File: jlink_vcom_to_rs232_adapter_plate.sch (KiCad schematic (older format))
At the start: 15 parts, among them J1 Conn_02x10_Odd_Even, J2 Conn_01x04, J3 Conn_02x10_Odd_Even, J4 Conn_01x06, J5 DB9_Male, J6 Conn_01x03, J7 Conn_01x03, U1 MAX232

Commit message: 1、增加 H7_TOOL 专用 SWD 接口 2、增加 XH-5A 接口
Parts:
- added J8: h7_tool_swd, Connector_JST:JST_XH_B5B-XH-A_1x05_P2.50mm_Vertical, symbol Connector_Generic:Conn_01x05
- added J9: Conn_01x05, Connector_JST:JST_XH_B5B-XH-A_1x05_P2.50mm_Vertical, symbol Connector_Generic:Conn_01x05
- U1: footprint Package_SO:SOP-16_4.55x10.3mm_P1.27mm -> Package_SO:SOP-16_4.4x10.4mm_P1.27mm
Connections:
- wire segments 76 -> 86
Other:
- moved on the sheet: J2, J4
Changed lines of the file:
@@
 EESchema Schematic File Version 4
+LIBS:jlink_vcom_to_rs232_adapter_plate-cache
 EELAYER 30 0
 EELAYER END
@@
 Comment4 ""
 $EndDescr
-$Comp
-L Connector_Generic:Conn_01x06 J4
-U 1 1 5DC2D3B1
-P 4050 4750
-F 0 "J4" H 4130 4742 50  0000 L CNN
-F 1 "Conn_01x06" H 4130 4651 50  0000 L CNN
-F 2 "Connector_JST:JST_XH_B6B-XH-A_1x06_P2.50mm_Vertical" H 4050 4750 50  0001 C CNN
-F 3 "~" H 4050 4750 50  0001 C CNN
-	1    4050 4750
-	1    0    0    -1
-$EndComp
 $Comp
 L power:GND #PWR02
@@
 F 0 "U1" H 6200 5050 50  0000 C CNN
 F 1 "MAX232" H 6250 4950 50  0000 C CNN
-F 2 "Package_SO:SOP-16_4.55x10.3mm_P1.27mm" H 6600 2800 50  0001 L CNN
+F 2 "Package_SO:SOP-16_4.4x10.4mm_P1.27mm" H 6600 2800 50  0001 L CNN
 F 3 "http://www.ti.com/lit/ds/symlink/max232.pdf" H 6550 3950 50  0001 C CNN
 	1    6550 3850
@@
 Wire Wire Line
 	7550 2950 7350 2950
-Wire Wire Line
-	7500 3250 7350 3250
 Wire Wire Line
 	8400 3450 7350 3450
@@
 Wire Wire Line
 	2050 4750 2500 4750
-Text Label 3400 4550 0    50   ~ 0
-VTref
-Wire Wire Line
-	3400 4550 3850 4550
-Wire Wire Line
-	3400 4650 3850 4650
-Wire Wire Line
-	3400 4750 3850 4750
-Wire Wire Line
-	3400 4850 3850 4850
-Wire Wire Line
-	3400 4950 3850 4950
 Text Label 2050 4650 0    50   ~ 0
 TMS
@@
 L Connector_Generic:Conn_01x04 J2
 U 1 1 5DC2CD47
-P 2700 4650
-F 0 "J2" H 2780 4642 50  0000 L CNN
-F 1 "Conn_01x04" H 2780 4551 50  0000 L CNN
-F 2 "Connector_JST:JST_XH_B4B-XH-A_1x04_P2.50mm_Vertical" H 2700 4650 50  0001 C CNN
-F 3 "~" H 2700 4650 50  0001 C CNN
-	1    2700 4650
-	1    0    0    -1
-$EndComp
-Wire Wire Line
-	2500 4850 2350 4850
+P 1850 4750
+F 0 "J2" H 1930 4742 50  0000 L CNN
+F 1 "Conn_01x04" H 1930 4651 50  0000 L CNN
+F 2 "Connector_JST:JST_XH_B4B-XH-A_1x04_P2.50mm_Vertical" H 1850 4750 50  0001 C CNN
+F 3 "~" H 1850 4750 50  0001 C CNN
+	1    1850 4750
+	-1   0    0    1
+$EndComp
 $Comp
 L power:GND #PWR01
 U 1 1 5DCC154F
-P 2350 4850
-F 0 "#PWR01" H 2350 4600 50  0001 C CNN
-F 1 "GND" V 2355 4722 50  0000 R CNN
-F 2 "" H 2350 4850 50  0001 C CNN
-F 3 "" H 2350 4850 50  0001 C CNN
-	1    2350 4850
-	0    1    1    0
-$EndComp
-Text Label 3400 4650 0    50   ~ 0
-TMS
-Text Label 3400 4750 0    50   ~ 0
-TCK
-Text Label 3400 4950 0    50   ~ 0
-nRESET
-$Comp
-L power:GND #PWR03
-U 1 1 5DCC1F1B
-P 3700 5050
-F 0 "#PWR03" H 3700 4800 50  0001 C CNN
-F 1 "GND" V 3705 4922 50  0000 R CNN
-F 2 "" H 3700 5050 50  0001 C CNN
-F 3 "" H 3700 5050 50  0001 C CNN
-	1    3700 5050
-	0    1    1    0
-$EndComp
-Wire Wire Line
-	3850 5050 3700 5050
-Text Label 3400 4850 0    50   ~ 0
-TDO
+P 2250 4850
+F 0 "#PWR01" H 2250 4600 50  0001 C CNN
+F 1 "GND" V 2255 4722 50  0000 R CNN
+F 2 "" H 2250 4850 50  0001 C CNN
+F 3 "" H 2250 4850 50  0001 C CNN
+	1    2250 4850
+	0    -1   -1   0
+$EndComp
 $Comp
 L Connector:DB9_Male J5
@@
 Wire Wire Line
 	7050 2450 7250 2450
+Wire Wire Line
+	7350 3250 7550 3250
+Wire Wire Line
+	2050 4850 2250 4850
+$Comp
+L power:GND #PWR0101
+U 1 1 5DC65388
+P 2250 5650
+F 0 "#PWR0101" H 2250 5400 50  0001 C CNN
+F 1 "GND" V 2255 5522 50  0000 R CNN
+F 2 "" H 2250 5650 50  0001 C CNN
+F 3 "" H 2250 5650 50  0001 C CNN
+	1    2250 5650
+	0    -1   -1   0
+$EndComp
+Text Label 2050 5350 0    50   ~ 0
+nRESET
+Text Label 2050 5450 0    50   ~ 0
+TCK
+Text Label 2050 5550 0    50   ~ 0
+TMS
+Wire Wire Line
+	2050 5550 2500 5550
+Wire Wire Line
+	2050 5450 2500 5450
+Wire Wire Line
+	2050 5350 2500 5350
+Text Label 2050 5750 0    50   ~ 0
+VTref
+$Comp
+L Connector_Generic:Conn_01x05 J8
+U 1 1 5DC5DBD3
+P 1850 5550
+F 0 "J8" H 2000 5550 50  0000 C CNN
+F 1 "h7_tool_swd" H 2150 5450 50  0000 C CNN
+F 2 "Connector_JST:JST_XH_B5B-XH-A_1x05_P2.50mm_Vertical" H 1850 5550 50  0001 C CNN
+F 3 "~" H 1850 5550 50  0001 C CNN
+	1    1850 5550
+	-1   0    0    1
+$EndComp
+Wire Wire Line
+	2050 5750 2500 5750
+Wire Wire Line
+	2050 5650 2250 5650
+$Comp
+L Connector_Generic:Conn_01x05 J9
+U 1 1 5DC95693
+P 3200 5550
+F 0 "J9" H 3350 5550 50  0000 C CNN
+F 1 "Conn_01x05" H 3500 5450 50  0000 C CNN
+F 2 "Connector_JST:JST_XH_B5B-XH-A_1x05_P2.50mm_Vertical" H 3200 5550 50  0001 C CNN
+F 3 "~" H 3200 5550 50  0001 C CNN
+	1    3200 5550
+	-1   0    0    1
+$EndComp
+Wire Wire Line
+	3400 5050 3600 5050
+Text Label 3400 4850 0    50   ~ 0
+TDO
+$Comp
+L power:GND #PWR03
+U 1 1 5DCC1F1B
+P 3600 5050
+F 0 "#PWR03" H 3600 4800 50  0001 C CNN
+F 1 "GND" V 3605 4922 50  0000 R CNN
+F 2 "" H 3600 5050 50  0001 C CNN
+F 3 "" H 3600 5050 50  0001 C CNN
+	1    3600 5050
+	0    -1   -1   0
+$EndComp
+Text Label 3400 4950 0    50   ~ 0
+nRESET
+Text Label 3400 4750 0    50   ~ 0
+TCK
+Text Label 3400 4650 0    50   ~ 0
+TMS
+Wire Wire Line
+	3400 4950 3850 4950
+Wire Wire Line
+	3400 4850 3850 4850
+Wire Wire Line
+	3400 4750 3850 4750
+Wire Wire Line
+	3400 4650 3850 4650
+Wire Wire Line
+	3400 4550 3850 4550
+Text Label 3400 4550 0    50   ~ 0
+VTref
+$Comp
+L Connector_Generic:Conn_01x06 J4
+U 1 1 5DC2D3B1
+P 3200 4850
+F 0 "J4" H 3280 4842 50  0000 L CNN
+F 1 "Conn_01x06" H 3280 4751 50  0000 L CNN
+F 2 "Connector_JST:JST_XH_B6B-XH-A_1x06_P2.50mm_Vertical" H 3200 4850 50  0001 C CNN
+F 3 "~" H 3200 4850 50  0001 C CNN
+	1    3200 4850
+	-1   0    0    1
+$EndComp
+$Comp
+L power:GND #PWR0102
+U 1 1 5DC9B28E
+P 3600 5750
+F 0 "#PWR0102" H 3600 5500 50  0001 C CNN
+F 1 "GND" V 3605 5622 50  0000 R CNN
+F 2 "" H 3600 5750 50  0001 C CNN
+F 3 "" H 3600 5750 50  0001 C CNN
+	1    3600 5750
+	0    -1   -1   0
+$EndComp
+Text Label 3400 5550 0    50   ~ 0
+TCK
+Text Label 3400 5450 0    50   ~ 0
+TMS
+Wire Wire Line
+	3400 5650 3850 5650
+Wire Wire Line
+	3400 5550 3850 5550
+Wire Wire Line
+	3400 5450 3850 5450
+Wire Wire Line
+	3400 5350 3850 5350
+Text Label 3400 5350 0    50   ~ 0
+VTref
+Text Label 3400 5650 0    50   ~ 0
+nRESET
+Wire Wire Line
+	3400 5750 3600 5750
 $EndSCHEMATC

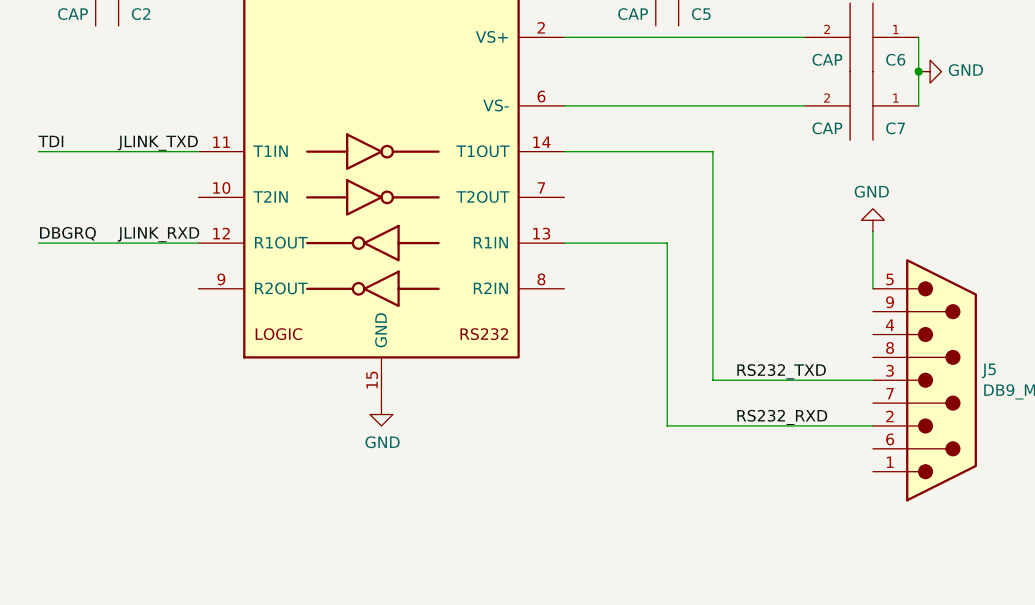
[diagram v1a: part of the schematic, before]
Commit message: 1、增加 电源 LED 灯 指示 2、布线 完成 3、泪滴 增加完成 4、覆铜 完成
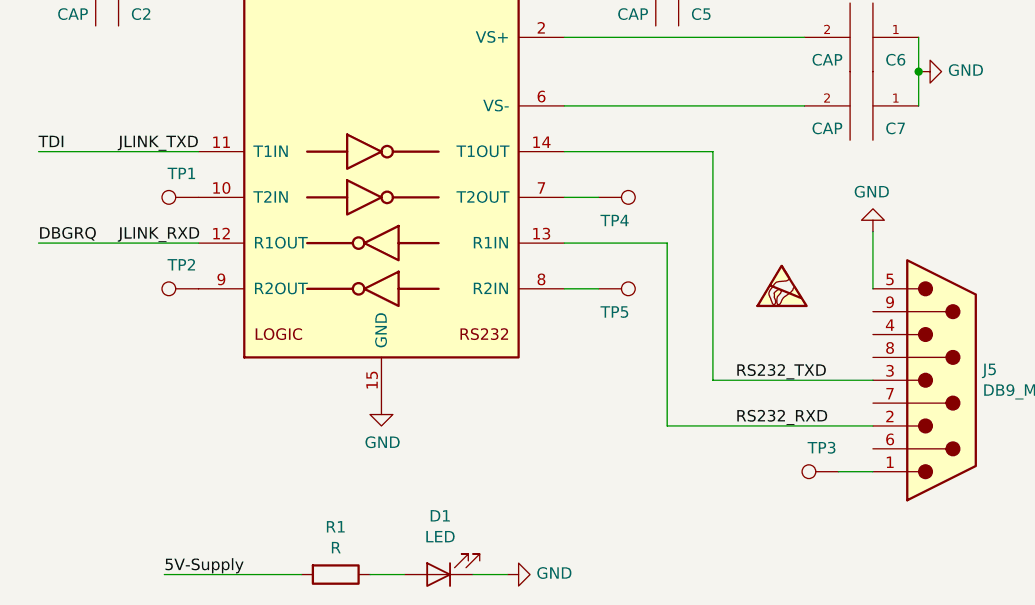
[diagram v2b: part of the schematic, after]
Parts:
- added D1: LED, LED_SMD:LED_0805_2012Metric, symbol Device:LED
- added R1: R, Resistor_SMD:R_0805_2012Metric, symbol Device:R
- added TP1, TP2, TP3, TP4, TP5: TestPoint, TestPoint:TestPoint_Pad_D1.0mm, symbol Connector:TestPoint
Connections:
- wire segments 86 -> 92
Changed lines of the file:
@@
 Wire Wire Line
 	3400 5750 3600 5750
+$Comp
+L Device:R R1
+U 1 1 5DC42984
+P 6350 5800
+F 0 "R1" V 6143 5800 50  0000 C CNN
+F 1 "R" V 6234 5800 50  0000 C CNN
+F 2 "Resistor_SMD:R_0805_2012Metric" V 6280 5800 50  0001 C CNN
+F 3 "~" H 6350 5800 50  0001 C CNN
+	1    6350 5800
+	0    1    1    0
+$EndComp
+$Comp
+L Device:LED D1
+U 1 1 5DC45839
+P 6800 5800
+F 0 "D1" H 6793 5545 50  0000 C CNN
+F 1 "LED" H 6793 5636 50  0000 C CNN
+F 2 "LED_SMD:LED_0805_2012Metric" H 6800 5800 50  0001 C CNN
+F 3 "~" H 6800 5800 50  0001 C CNN
+	1    6800 5800
+	-1   0    0    1
+$EndComp
+$Comp
+L power:GND #PWR0103
+U 1 1 5DC46F08
+P 7100 5800
+F 0 "#PWR0103" H 7100 5550 50  0001 C CNN
+F 1 "GND" V 7105 5672 50  0000 R CNN
+F 2 "" H 7100 5800 50  0001 C CNN
+F 3 "" H 7100 5800 50  0001 C CNN
+	1    7100 5800
+	0    -1   -1   0
+$EndComp
+Wire Wire Line
+	7100 5800 6950 5800
+Wire Wire Line
+	6650 5800 6500 5800
+Wire Wire Line
+	5600 5800 6200 5800
+Text Label 5600 5800 0    50   ~ 0
+5V-Supply
+$Comp
+L Connector:TestPoint TP2
+U 1 1 5DC86AE9
+P 5750 4550
+F 0 "TP2" V 5853 4622 50  0000 C CNN
+F 1 "TestPoint" V 5854 4622 50  0001 C CNN
+F 2 "TestPoint:TestPoint_Pad_D1.0mm" H 5950 4550 50  0001 C CNN
+F 3 "~" H 5950 4550 50  0001 C CNN
+	1    5750 4550
+	0    -1   -1   0
+$EndComp
+$Comp
+L Connector:TestPoint TP1
+U 1 1 5DC88682
+P 5750 4150
+F 0 "TP1" V 5853 4222 50  0000 C CNN
+F 1 "TestPoint" V 5854 4222 50  0001 C CNN
+F 2 "TestPoint:TestPoint_Pad_D1.0mm" H 5950 4150 50  0001 C CNN
+F 3 "~" H 5950 4150 50  0001 C CNN
+	1    5750 4150
+	0    -1   -1   0
+$EndComp
+$Comp
+L Connector:TestPoint TP3
+U 1 1 5DC89304
+P 8550 5350
+F 0 "TP3" V 8653 5422 50  0000 C CNN
+F 1 "TestPoint" V 8654 5422 50  0001 C CNN
+F 2 "TestPoint:TestPoint_Pad_D1.0mm" H 8750 5350 50  0001 C CNN
+F 3 "~" H 8750 5350 50  0001 C CNN
+	1    8550 5350
+	0    -1   -1   0
+$EndComp
+Wire Wire Line
+	8700 5350 8550 5350
+$Comp
+L Connector:TestPoint TP4
+U 1 1 5DC97FF8
+P 7500 4150
+F 0 "TP4" V 7603 4222 50  0000 C CNN
+F 1 "TestPoint" V 7604 4222 50  0001 C CNN
+F 2 "TestPoint:TestPoint_Pad_D1.0mm" H 7700 4150 50  0001 C CNN
+F 3 "~" H 7700 4150 50  0001 C CNN
+	1    7500 4150
+	0    1    1    0
+$EndComp
+$Comp
+L Connector:TestPoint TP5
+U 1 1 5DC9890A
+P 7500 4550
+F 0 "TP5" V 7603 4622 50  0000 C CNN
+F 1 "TestPoint" V 7604 4622 50  0001 C CNN
+F 2 "TestPoint:TestPoint_Pad_D1.0mm" H 7700 4550 50  0001 C CNN
+F 3 "~" H 7700 4550 50  0001 C CNN
+	1    7500 4550
+	0    1    1    0
+$EndComp
+Wire Wire Line
+	7500 4150 7350 4150
+Wire Wire Line
+	7500 4550 7350 4550
+$Comp
+L Graphic:SYM_ESD_Small #SYM1
+U 1 1 5DCB5DFD
+P 8300 4550
+F 0 "#SYM1" H 8300 4690 50  0001 C CNN
+F 1 "SYM_ESD_Small" H 8300 4425 50  0001 C CNN
+F 2 "" H 8300 4560 50  0001 C CNN
+F 3 "~" H 8300 4560 50  0001 C CNN
+	1    8300 4550
+	1    0    0    -1
+$EndComp
 $EndSCHEMATC

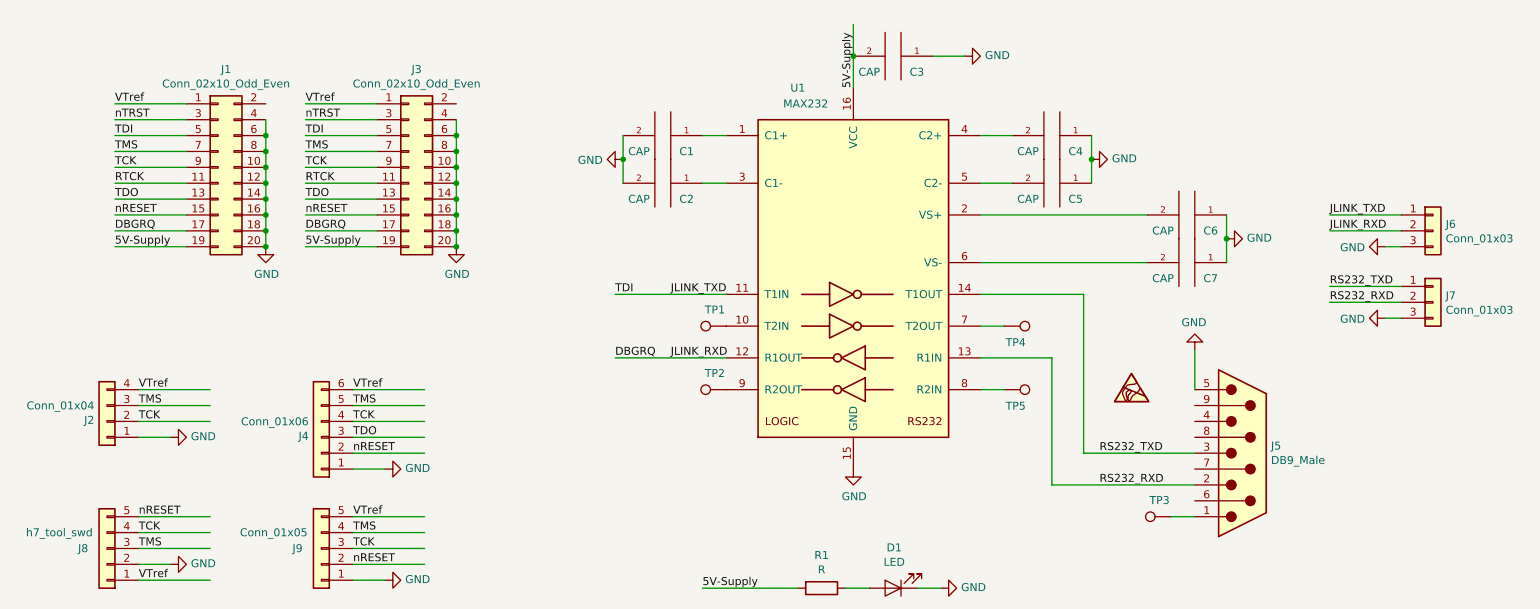
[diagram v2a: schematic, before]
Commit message: 1、修改 每个 元器件 为实际的 value 2、生成了 geber 文件
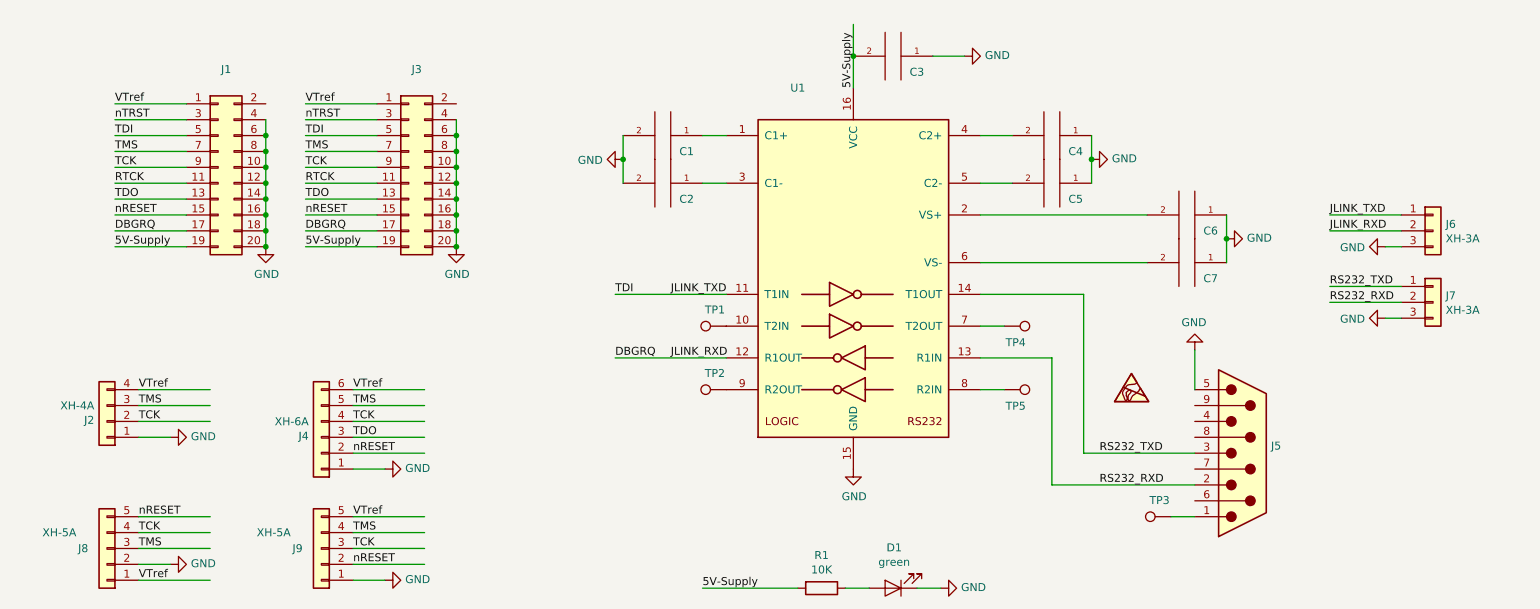
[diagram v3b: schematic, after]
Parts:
- C1, C2, C3, C4, C5, C6, C7: value CAP -> 220nF(224) ±10% 16V
- D1: value LED -> green
- J1: value Conn_02x10_Odd_Even -> 排母 2*10P 2.54mm 弯针
- J2: value Conn_01x04 -> XH-4A
- J3: value Conn_02x10_Odd_Even -> 2.54mm 2*10P 直 简牛
- J4: value Conn_01x06 -> XH-6A
- J5: value DB9_Male -> DMR-XP 公头叉锁 9P 半金
- J6, J7: value Conn_01x03 -> XH-3A
- J8: value h7_tool_swd -> XH-5A
- J9: value Conn_01x05 -> XH-5A
- R1: value R -> 10K
- U1: value MAX232 -> UT3232G-S16-R
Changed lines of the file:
@@
 P 3750 3150
 F 0 "J3" H 3800 3767 50  0000 C CNN
-F 1 "Conn_02x10_Odd_Even" H 3800 3676 50  0000 C CNN
+F 1 "2.54mm 2*10P 直 简牛" H 3800 3676 50  0001 C CNN
 F 2 "Connector_IDC:IDC-Header_2x10_P2.54mm_Vertical" H 3750 3150 50  0001 C CNN
 F 3 "~" H 3750 3150 50  0001 C CNN
@@
 P 2550 3150
 F 0 "J1" H 2600 3767 50  0000 C CNN
-F 1 "Conn_02x10_Odd_Even" H 2600 3676 50  0000 C CNN
+F 1 "排母 2*10P 2.54mm 弯针" H 2600 3676 50  0001 C CNN
 F 2 "Connector_PinSocket_2.54mm:PinSocket_2x10_P2.54mm_Horizontal" H 2550 3150 50  0001 C CNN
 F 3 "~" H 2550 3150 50  0001 C CNN
@@
 P 6550 3850
 F 0 "U1" H 6200 5050 50  0000 C CNN
-F 1 "MAX232" H 6250 4950 50  0000 C CNN
+F 1 "UT3232G-S16-R" H 6250 4950 50  0001 C CNN
 F 2 "Package_SO:SOP-16_4.4x10.4mm_P1.27mm" H 6600 2800 50  0001 L CNN
 F 3 "http://www.ti.com/lit/ds/symlink/max232.pdf" H 6550 3950 50  0001 C CNN
@@
 P 5350 3250
 F 0 "C2" V 5450 3400 50  0000 C CNN
-F 1 "CAP" V 5450 3100 50  0000 C CNN
+F 1 "220nF(224) ±10% 16V" V 5450 3100 50  0001 C CNN
 F 2 "Capacitor_SMD:C_0805_2012Metric" H 5350 3250 50  0001 C CNN
 F 3 "~" H 5350 3250 50  0001 C CNN
@@
 P 5350 2950
 F 0 "C1" V 5450 3100 50  0000 C CNN
-F 1 "CAP" V 5450 2800 50  0000 C CNN
+F 1 "220nF(224) ±10% 16V" V 5450 2800 50  0001 C CNN
 F 2 "Capacitor_SMD:C_0805_2012Metric" H 5350 2950 50  0001 C CNN
 F 3 "~" H 5350 2950 50  0001 C CNN
@@
 P 7800 2950
 F 0 "C4" V 7900 3100 50  0000 C CNN
-F 1 "CAP" V 7900 2800 50  0000 C CNN
+F 1 "220nF(224) ±10% 16V" V 7900 2800 50  0001 C CNN
 F 2 "Capacitor_SMD:C_0805_2012Metric" H 7800 2950 50  0001 C CNN
 F 3 "~" H 7800 2950 50  0001 C CNN
@@
 P 7800 3250
 F 0 "C5" V 7900 3400 50  0000 C CNN
-F 1 "CAP" V 7900 3100 50  0000 C CNN
+F 1 "220nF(224) ±10% 16V" V 7900 3100 50  0001 C CNN
 F 2 "Capacitor_SMD:C_0805_2012Metric" H 7800 3250 50  0001 C CNN
 F 3 "~" H 7800 3250 50  0001 C CNN
@@
 P 8650 3450
 F 0 "C6" V 8750 3600 50  0000 C CNN
-F 1 "CAP" V 8750 3300 50  0000 C CNN
+F 1 "220nF(224) ±10% 16V" V 8750 3300 50  0001 C CNN
 F 2 "Capacitor_SMD:C_0805_2012Metric" H 8650 3450 50  0001 C CNN
 F 3 "~" H 8650 3450 50  0001 C CNN
@@
 P 8650 3750
 F 0 "C7" V 8750 3900 50  0000 C CNN
-F 1 "CAP" V 8750 3600 50  0000 C CNN
+F 1 "220nF(224) ±10% 16V" V 8750 3600 50  0001 C CNN
 F 2 "Capacitor_SMD:C_0805_2012Metric" H 8650 3750 50  0001 C CNN
 F 3 "~" H 8650 3750 50  0001 C CNN
@@
 P 1850 4750
 F 0 "J2" H 1930 4742 50  0000 L CNN
-F 1 "Conn_01x04" H 1930 4651 50  0000 L CNN
+F 1 "XH-4A" H 1930 4651 50  0000 L CNN
 F 2 "Connector_JST:JST_XH_B4B-XH-A_1x04_P2.50mm_Vertical" H 1850 4750 50  0001 C CNN
 F 3 "~" H 1850 4750 50  0001 C CNN
@@
 P 9000 4950
 F 0 "J5" H 9180 4996 50  0000 L CNN
-F 1 "DB9_Male" H 9180 4905 50  0000 L CNN
+F 1 "DMR-XP 公头叉锁 9P 半金" H 9180 4905 50  0001 L CNN
 F 2 "Connector_Dsub:DSUB-9_Male_Horizontal_P2.77x2.84mm_EdgePinOffset9.90mm_Housed_MountingHolesOffset11.32mm" H 9000 4950 50  0001 C CNN
 F 3 " ~" H 9000 4950 50  0001 C CNN
@@
 P 10200 4000
 F 0 "J7" H 10280 4042 50  0000 L CNN
-F 1 "Conn_01x03" H 10280 3951 50  0000 L CNN
+F 1 "XH-3A" H 10280 3951 50  0000 L CNN
 F 2 "Connector_JST:JST_XH_B3B-XH-A_1x03_P2.50mm_Vertical" H 10200 4000 50  0001 C CNN
 F 3 "~" H 10200 4000 50  0001 C CNN
@@
 P 10200 3550
 F 0 "J6" H 10280 3592 50  0000 L CNN
-F 1 "Conn_01x03" H 10280 3501 50  0000 L CNN
+F 1 "XH-3A" H 10280 3501 50  0000 L CNN
 F 2 "Connector_JST:JST_XH_B3B-XH-A_1x03_P2.50mm_Vertical" H 10200 3550 50  0001 C CNN
 F 3 "~" H 10200 3550 50  0001 C CNN
@@
 P 6800 2450
 F 0 "C3" V 6900 2600 50  0000 C CNN
-F 1 "CAP" V 6900 2300 50  0000 C CNN
+F 1 "220nF(224) ±10% 16V" V 6900 2300 50  0001 C CNN
 F 2 "Capacitor_SMD:C_0805_2012Metric" H 6800 2450 50  0001 C CNN
 F 3 "~" H 6800 2450 50  0001 C CNN
@@
 P 1850 5550
 F 0 "J8" H 2000 5550 50  0000 C CNN
-F 1 "h7_tool_swd" H 2150 5450 50  0000 C CNN
+F 1 "XH-5A" H 2150 5450 50  0000 C CNN
 F 2 "Connector_JST:JST_XH_B5B-XH-A_1x05_P2.50mm_Vertical" H 1850 5550 50  0001 C CNN
 F 3 "~" H 1850 5550 50  0001 C CNN
@@
 P 3200 5550
 F 0 "J9" H 3350 5550 50  0000 C CNN
-F 1 "Conn_01x05" H 3500 5450 50  0000 C CNN
+F 1 "XH-5A" H 3500 5450 50  0000 C CNN
 F 2 "Connector_JST:JST_XH_B5B-XH-A_1x05_P2.50mm_Vertical" H 3200 5550 50  0001 C CNN
 F 3 "~" H 3200 5550 50  0001 C CNN
@@
 P 3200 4850
 F 0 "J4" H 3280 4842 50  0000 L CNN
-F 1 "Conn_01x06" H 3280 4751 50  0000 L CNN
+F 1 "XH-6A" H 3280 4751 50  0000 L CNN
 F 2 "Connector_JST:JST_XH_B6B-XH-A_1x06_P2.50mm_Vertical" H 3200 4850 50  0001 C CNN
 F 3 "~" H 3200 4850 50  0001 C CNN
@@
 P 6350 5800
 F 0 "R1" V 6143 5800 50  0000 C CNN
-F 1 "R" V 6234 5800 50  0000 C CNN
+F 1 "10K" V 6234 5800 50  0000 C CNN
 F 2 "Resistor_SMD:R_0805_2012Metric" V 6280 5800 50  0001 C CNN
 F 3 "~" H 6350 5800 50  0001 C CNN
@@
 P 6800 5800
 F 0 "D1" H 6793 5545 50  0000 C CNN
-F 1 "LED" H 6793 5636 50  0000 C CNN
+F 1 "green" H 6793 5636 50  0000 C CNN
 F 2 "LED_SMD:LED_0805_2012Metric" H 6800 5800 50  0001 C CNN
 F 3 "~" H 6800 5800 50  0001 C CNN
